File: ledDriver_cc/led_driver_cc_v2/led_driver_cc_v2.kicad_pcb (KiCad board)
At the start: 2 copper layers, 97 x 72 mm, 21 parts, among them J1 Conn_01x08_Pin, J3 Conn_01x02_Female, U1 TSR_1-2490, U2 WeMos_D1_mini

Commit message: add partslib
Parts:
- removed U7: ~, Package_SO:SOIC-8_3.9x4.9mm_P1.27mm
- added ESP32_S1: ~, custom_footprints:ESP32-S3-Zero, F.Cu at (101.4, 124.5)
- added H1: MountingHole, MountingHole:MountingHole_2.7mm_M2.5_DIN965_Pad_TopBottom, F.Cu at (92.9, 89.5)
- added H2: MountingHole, MountingHole:MountingHole_2.7mm_M2.5_DIN965_Pad_TopBottom, F.Cu at (175.9, 138.5)
- added H3: MountingHole, MountingHole:MountingHole_2.7mm_M2.5_DIN965_Pad_TopBottom, F.Cu at (175.9, 89.5)
- added H4: MountingHole, MountingHole:MountingHole_2.7mm_M2.5_DIN965_Pad_TopBottom, F.Cu at (92.9, 139.0)
- U2: value WeMos_D1_mini -> LM3404; footprint Module:WEMOS_D1_mini_light -> Package_SO:SOIC-8_3.9x4.9mm_P1.27mm
- moved C14 71.2 mm to (139.4, 134.9)
- moved R19 65.3 mm to (145.9, 123.0), turned to 180 degrees
- moved U2 59.6 mm to (146.2, 130.0), turned to 90 degrees
- moved C11 58.4 mm to (135.4, 134.5)
- moved C1 48.2 mm to (102.4, 109.5)
- moved R3 47.0 mm to (162.9, 127.5)
- moved C12 43.5 mm to (102.4, 111.1)
- moved C10 35.8 mm to (94.8, 109.4)
- moved C13 35.8 mm to (99.4, 109.5)
- moved D2 26.7 mm to (146.1, 137.5)
- moved L2 25.4 mm to (157.9, 135.5)
- moved C2 19.3 mm to (122.8, 94.5)
- moved C3 19.3 mm to (129.3, 109.7)
- moved C4 19.3 mm to (136.8, 94.5)
- moved C5 19.3 mm to (122.3, 110.5)
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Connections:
- C1 pad 1: Net-(U7-VCC) -> Net-(U2-VCC)
- C14 pad 1: Net-(U7-BOOT) -> Net-(U2-BOOT)
- C3 pad 1: VCC -> +5V
- C5 pad 1: VCC -> +5V
- R19 pad 1: Net-(U7-RON) -> Net-(U2-RON)
- U1 pad 3: VCC -> +5V
- U2 pad 1: unconnected-(U2-~{RST}-Pad1) -> Net-(D2-K)
- U2 pad 2: unconnected-(U2-A0-Pad2) -> Net-(U2-BOOT)
- U2 pad 3: unconnected-(U2-D0-Pad3) -> PWM3
- U2 pad 4: unconnected-(U2-SCK/D5-Pad4) -> GND
- U2 pad 6: unconnected-(U2-MOSI/D7-Pad6) -> Net-(U2-RON)
- U2 pad 7: unconnected-(U2-CS/D8-Pad7) -> Net-(U2-VCC)
- U2 pad 8: unconnected-(U2-3V3-Pad8) -> VCC
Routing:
- net Net-(D2-K): track 0.00 -> 16.0 mm
- net VCC: track 0.00 -> 4.75 mm
- net Net-(U2-RON): track 0.00 -> 4.53 mm
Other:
- board size 97 x 72 mm -> 89 x 55.5 mm

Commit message: more custom parts
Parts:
- F1: footprint Fuse:Fuseholder_Littelfuse_Nano2_154x -> custom_footprints:Fuse_Littelfuse-NANO2-451_453
- L2: footprint Inductor_SMD:L_10.4x10.4_H4.8 -> Inductor_SMD:L_TDK_SLF10145
- moved F1 0.80 mm to (108.4, 95.0)

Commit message: removed lib
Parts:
- C2: footprint Capacitor_THT:CP_Radial_D13.0mm_P5.00mm -> Capacitor_SMD:CP_Elec_10x10
- moved C4 4.98 mm to (141.8, 94.5)
- moved R3 4.83 mm to (158.1, 127.2)
- moved C2 4.43 mm to (123.3, 98.9)
- moved ESP32_S1 3.61 mm to (105.0, 124.9)
- moved J3 2.19 mm to (95.3, 101.8)

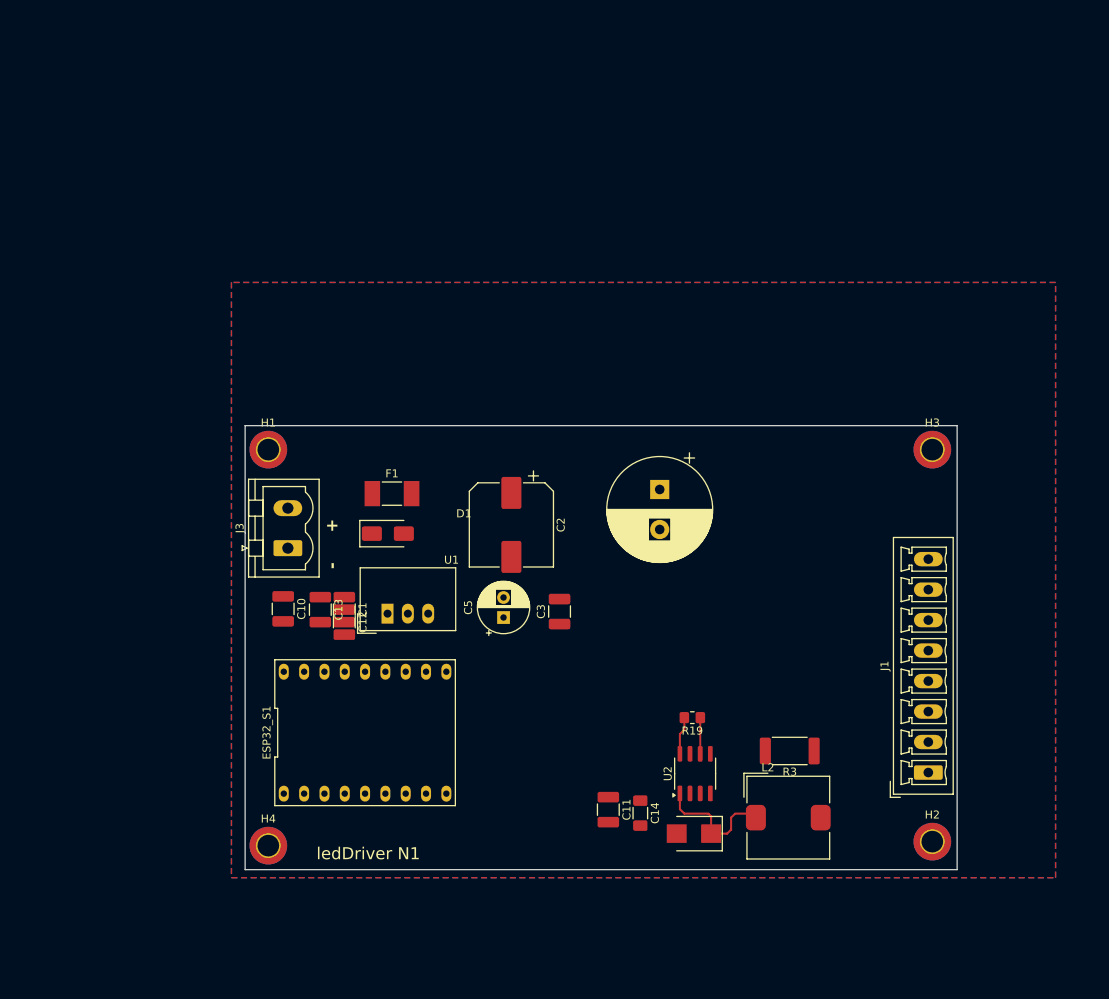
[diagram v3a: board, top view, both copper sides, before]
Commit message: add new channels to led driver
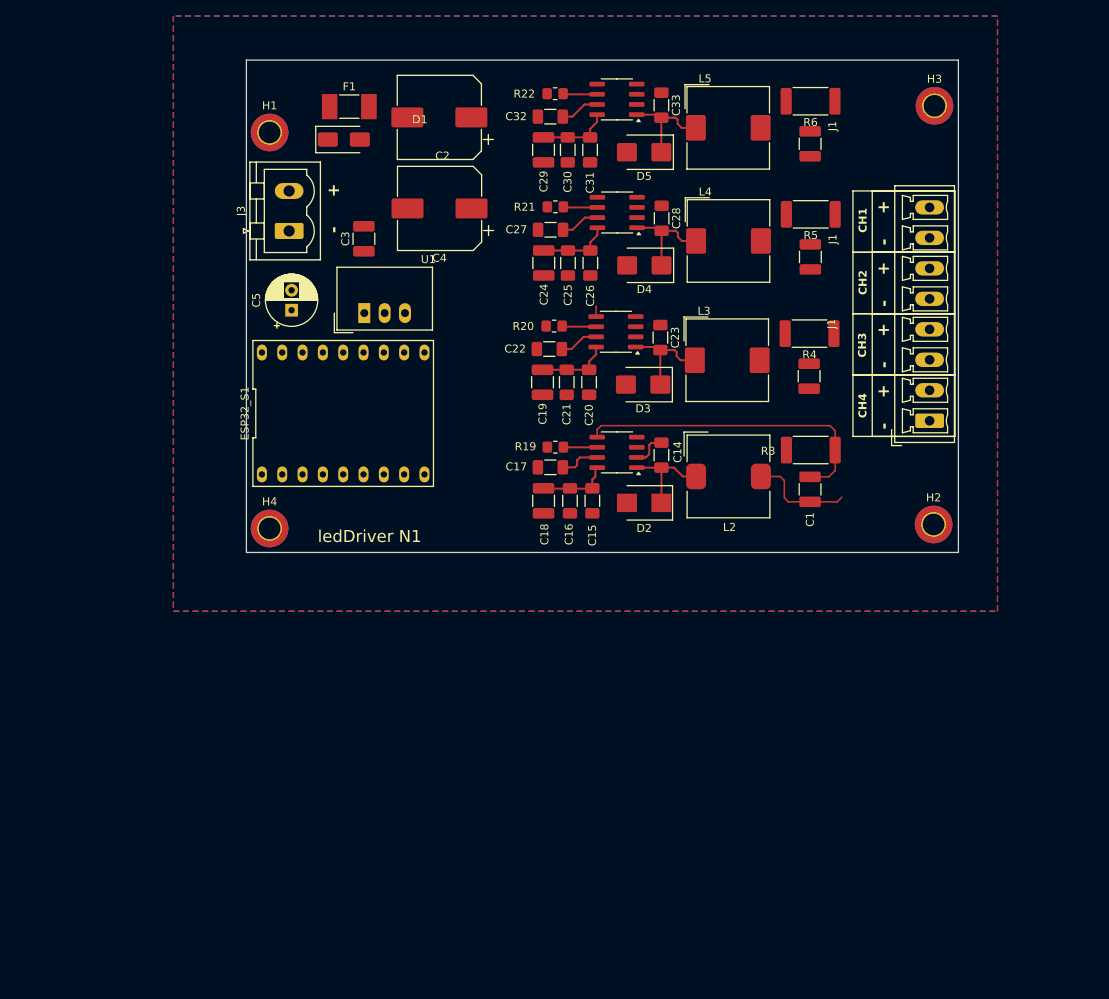
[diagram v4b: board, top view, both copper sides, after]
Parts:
- removed C10, C11, C12, C13: C, Capacitor_SMD:C_1210_3225Metric_Pad1.33x2.70mm_HandSolder
- added C15: 2,2UF, Capacitor_SMD:C_1206_3216Metric_Pad1.33x1.80mm_HandSolder, F.Cu at (133.4, 95.9)
- added C16: 100nF, Capacitor_SMD:C_1206_3216Metric_Pad1.33x1.80mm_HandSolder, F.Cu at (130.6, 95.9)
- added C17: 100nF, Capacitor_SMD:C_1206_3216Metric_Pad1.33x1.80mm_HandSolder, F.Cu at (128.2, 91.7)
- added C18: 10uF, Capacitor_SMD:C_1210_3225Metric_Pad1.33x2.70mm_HandSolder, F.Cu at (127.3, 95.9)
- added C19: 10uF, Capacitor_SMD:C_1210_3225Metric_Pad1.33x2.70mm_HandSolder, F.Cu at (127.2, 81.1)
- added C20: 2,2UF, Capacitor_SMD:C_1206_3216Metric_Pad1.33x1.80mm_HandSolder, F.Cu at (133.0, 81.1)
- added C21: 100nF, Capacitor_SMD:C_1206_3216Metric_Pad1.33x1.80mm_HandSolder, F.Cu at (130.2, 81.1)
- added C22: 100nF, Capacitor_SMD:C_1206_3216Metric_Pad1.33x1.80mm_HandSolder, F.Cu at (128.0, 76.9)
- added C23: 10nF, Capacitor_SMD:C_1206_3216Metric_Pad1.33x1.80mm_HandSolder, F.Cu at (141.9, 75.5)
- added C24: 10uF, Capacitor_SMD:C_1210_3225Metric_Pad1.33x2.70mm_HandSolder, F.Cu at (127.3, 66.2)
- added C25: 2,2UF, Capacitor_SMD:C_1206_3216Metric_Pad1.33x1.80mm_HandSolder, F.Cu at (130.4, 66.2)
- added C26: 100nF, Capacitor_SMD:C_1206_3216Metric_Pad1.33x1.80mm_HandSolder, F.Cu at (133.2, 66.2)
- added C27: 100nF, Capacitor_SMD:C_1206_3216Metric_Pad1.33x1.80mm_HandSolder, F.Cu at (128.2, 62.0)
- added C28: 10nF, Capacitor_SMD:C_1206_3216Metric_Pad1.33x1.80mm_HandSolder, F.Cu at (142.1, 60.6)
- added C29: 10uF, Capacitor_SMD:C_1210_3225Metric_Pad1.33x2.70mm_HandSolder, F.Cu at (127.3, 52.0)
- added C30: 2,2UF, Capacitor_SMD:C_1206_3216Metric_Pad1.33x1.80mm_HandSolder, F.Cu at (130.3, 52.0)
- added C31: 100nF, Capacitor_SMD:C_1206_3216Metric_Pad1.33x1.80mm_HandSolder, F.Cu at (133.1, 52.0)
- added C32: 100nF, Capacitor_SMD:C_1206_3216Metric_Pad1.33x1.80mm_HandSolder, F.Cu at (128.2, 47.9)
- added C33: 10nF, Capacitor_SMD:C_1206_3216Metric_Pad1.33x1.80mm_HandSolder, F.Cu at (142.0, 46.4)
- added C6: 470nF, Capacitor_SMD:C_1210_3225Metric_Pad1.33x2.70mm_HandSolder, F.Cu at (160.5, 80.3)
- added C7: 470nF, Capacitor_SMD:C_1210_3225Metric_Pad1.33x2.70mm_HandSolder, F.Cu at (160.7, 65.4)
- added C8: 470nF, Capacitor_SMD:C_1210_3225Metric_Pad1.33x2.70mm_HandSolder, F.Cu at (160.6, 51.3)
- added D3: D_Schottky, Diode_SMD:D_SMB, F.Cu at (139.7, 81.4)
- added D4: D_Schottky, Diode_SMD:D_SMB, F.Cu at (139.9, 66.5)
- added D5: D_Schottky, Diode_SMD:D_SMB, F.Cu at (139.9, 52.3)
- added L3: 47µH, Inductor_SMD:L_TDK_SLF10145, F.Cu at (150.3, 78.3)
- added L4: 47µH, Inductor_SMD:L_TDK_SLF10145, F.Cu at (150.4, 63.4)
- added L5: 47µH, Inductor_SMD:L_TDK_SLF10145, F.Cu at (150.4, 49.3)
- added R20: 536k, Resistor_SMD:R_0805_2012Metric_Pad1.20x1.40mm_HandSolder, F.Cu at (128.6, 74.1)
- added R21: 536k, Resistor_SMD:R_0805_2012Metric_Pad1.20x1.40mm_HandSolder, F.Cu at (128.8, 59.1)
- added R22: 536k, Resistor_SMD:R_0805_2012Metric_Pad1.20x1.40mm_HandSolder, F.Cu at (128.8, 45.0)
- added R4: 0.2R, Resistor_SMD:R_2512_6332Metric_Pad1.40x3.35mm_HandSolder, F.Cu at (160.6, 75.0)
- added R5: 0.2R, Resistor_SMD:R_2512_6332Metric_Pad1.40x3.35mm_HandSolder, F.Cu at (160.7, 60.1)
- added R6: 0.2R, Resistor_SMD:R_2512_6332Metric_Pad1.40x3.35mm_HandSolder, F.Cu at (160.7, 45.9)
- added U3: LM3404, Package_SO:SOIC-8_3.9x4.9mm_P1.27mm, F.Cu at (136.4, 74.8)
- added U4: LM3404, Package_SO:SOIC-8_3.9x4.9mm_P1.27mm, F.Cu at (136.5, 59.9)
- added U5: LM3404, Package_SO:SOIC-8_3.9x4.9mm_P1.27mm, F.Cu at (136.5, 45.7)
- C1: value C -> 470nF
- C14: value C -> 10nF
- C4: footprint Capacitor_THT:CP_Radial_D13.0mm_P5.00mm -> Capacitor_SMD:CP_Elec_10x10
- L2: value L -> 47µH
- R19: value R -> 536k
- R3: value R -> 0.2R
- moved C1 60.1 mm to (160.6, 94.5), turned to 90 degrees
- moved C3 52.6 mm to (104.8, 63.1)
- moved C2 51.7 mm to (114.3, 48.0), turned to 180 degrees
- moved D1 49.6 mm to (102.3, 50.7)
- moved F1 48.7 mm to (103.0, 46.6)
- moved C5 46.7 mm to (95.8, 72.1)
- moved C14 44.8 mm to (142.0, 90.2)
- moved C4 44.6 mm to (114.3, 59.3), turned to 180 degrees
- moved J1 44.0 mm to (175.6, 85.9)
- moved L2 43.3 mm to (150.4, 92.9)
- moved H3 43.0 mm to (176.2, 46.5)
- moved D2 41.8 mm to (139.9, 96.2)
- moved U2 41.3 mm to (136.5, 89.8), turned to 180 degrees
- moved ESP32_S1 40.0 mm to (102.3, 85.0)
- moved H1 39.6 mm to (93.1, 49.9)
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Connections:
- net Net-(D2-K) renamed /U2_SW
- net Net-(U2-BOOT) renamed /U2_BOOT
- net PWM4 renamed PWM_CH4
- C1 pad 1: Net-(U2-VCC) -> LED_CH1+
- C1 pad 2: GND -> LED_CH1-
- ESP32_S1 pad 14: PWM3 -> PWM_CH3
- ESP32_S1 pad 15: PWM2 -> PWM_CH2
- ESP32_S1 pad 16: PWM1 -> PWM_CH1
- L2 pad 2: LED3+ -> LED_CH1+
- R3 pad 1: LED3- -> LED_CH1-
- U2 pad 3: PWM3 -> PWM_CH1
- U2 pad 5: unconnected-(U2-CS-Pad5) -> LED_CH1-
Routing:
- net LED_CH1-: track 0.00 -> 39.6 mm
- net VCC: track 4.75 -> 36.1 mm
- net /U4_SW: track 0.00 -> 25.4 mm
- net LED_CH1+: track 0.00 -> 12.9 mm
- net /U3_SW: track 0.00 -> 12.7 mm
- net Net-(U2-VCC): track 0.00 -> 4.95 mm
- net /U2_BOOT: track 0.00 -> 4.74 mm
- net Net-(U3-VCC): track 0.00 -> 4.54 mm
- net Net-(U5-VCC): track 0.00 -> 4.54 mm
- net Net-(U4-VCC): track 0.00 -> 4.54 mm
- net Net-(U4-RON): track 0.00 -> 4.36 mm
- net Net-(U3-RON): track 0.00 -> 4.36 mm
- net Net-(U5-RON): track 0.00 -> 4.36 mm
- net /U2_SW: track 16.0 -> 12.4 mm
- net LED_CH2-: track 0.00 -> 1.28 mm
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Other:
- board size 89 x 55.5 mm -> 89 x 61.5 mm
- board text added: "CH1"
- board text added: "CH2"
- board text added: "CH3"
- board text added: "CH4"
- board text added: "J1"

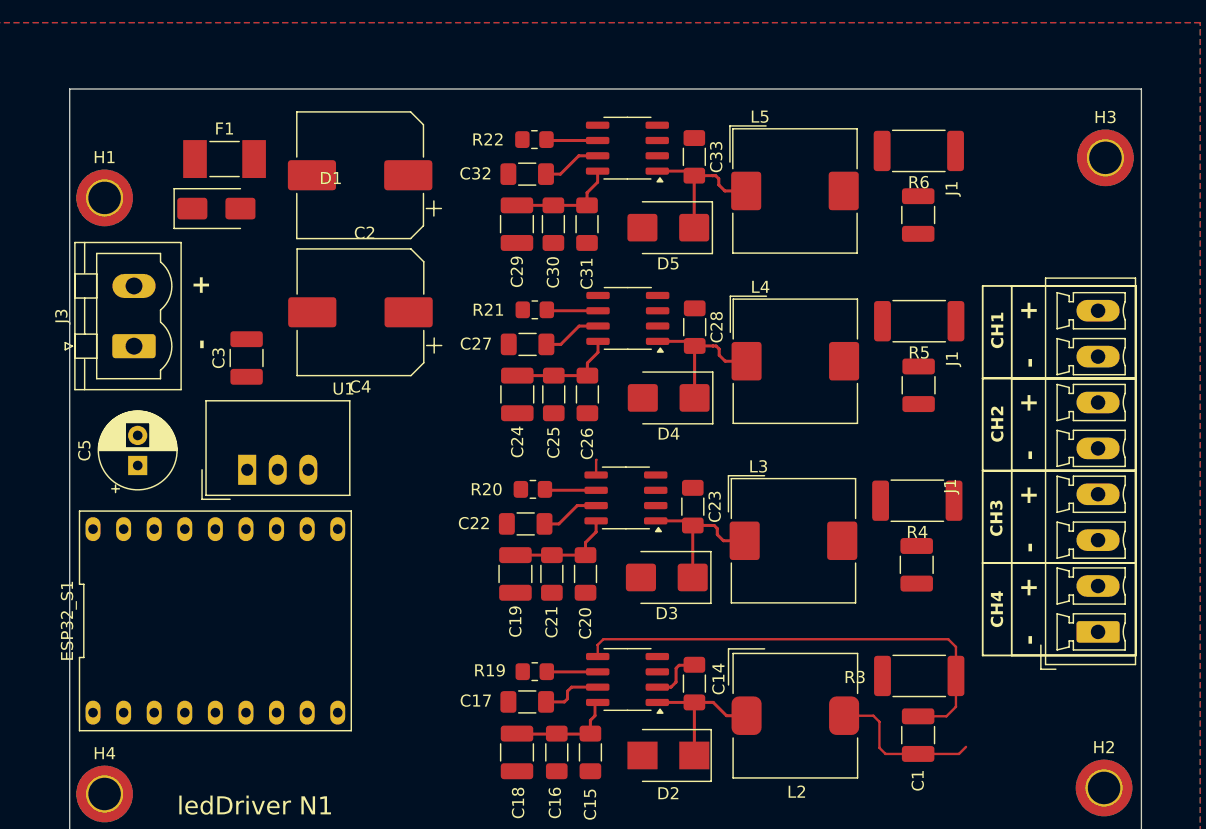
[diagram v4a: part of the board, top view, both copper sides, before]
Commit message: new channel arrangement
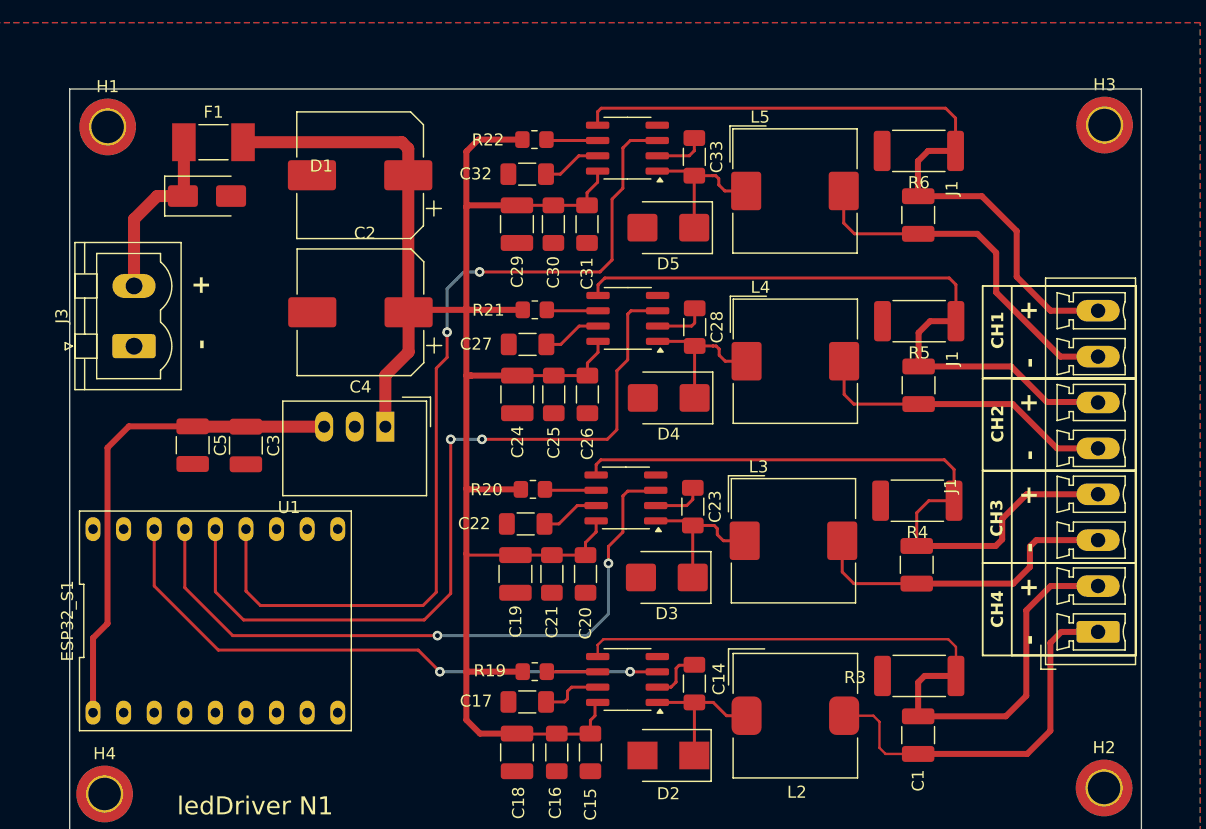
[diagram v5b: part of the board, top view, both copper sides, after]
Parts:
- C5: value C_Polarized -> C; footprint Capacitor_THT:CP_Radial_D6.3mm_P2.50mm -> Capacitor_SMD:C_1210_3225Metric_Pad1.33x2.70mm_HandSolder
- moved U1 12.0 mm to (116.4, 68.8), turned to 180 degrees
- moved C3 7.27 mm to (104.8, 70.4), turned to -90 degrees
- moved H1 5.90 mm to (93.3, 44.0)
- moved C5 4.87 mm to (100.4, 70.4), turned to -90 degrees
- moved H3 2.72 mm to (176.1, 43.8)
- moved F1 1.67 mm to (102.1, 45.2)
- moved D1 1.30 mm to (101.6, 49.7)
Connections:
- C1 pad 1: LED_CH1+ -> LED_CH4+
- C1 pad 2: LED_CH1- -> LED_CH4-
- C2 pad 1: Net-(U1-Vin) -> VCC
- C33 pad 1: /U4_BOOT -> /U5_BOOT
- C33 pad 2: /U4_SW -> /U5_SW
- C4 pad 1: Net-(U1-Vin) -> VCC
- C6 pad 1: LED_CH2+ -> LED_CH3+
- C6 pad 2: LED_CH2- -> LED_CH3-
- C7 pad 1: LED_CH3+ -> LED_CH2+
- C7 pad 2: LED_CH3- -> LED_CH2-
- C8 pad 1: LED_CH3+ -> LED_CH1+
- C8 pad 2: LED_CH3- -> LED_CH1-
- D5 pad 1: /U4_SW -> /U5_SW
- F1 pad 2: Net-(U1-Vin) -> VCC
- J1 pad 1: LED3- -> LED_CH4+
- J1 pad 2: LED3+ -> LED_CH4-
- J1 pad 3: LED4- -> LED_CH3+
- J1 pad 4: LED4+ -> LED_CH3-
- J1 pad 5: LED2+ -> LED_CH2+
- J1 pad 6: LED2- -> LED_CH2-
- J1 pad 7: LED1+ -> LED_CH1+
- J1 pad 8: LED1- -> LED_CH1-
- L2 pad 2: LED_CH1+ -> LED_CH4+
- L3 pad 2: LED_CH2+ -> LED_CH3+
- L4 pad 2: LED_CH3+ -> LED_CH2+
- L5 pad 1: /U4_SW -> /U5_SW
- L5 pad 2: LED_CH3+ -> LED_CH1+
- R3 pad 1: LED_CH1- -> LED_CH4-
- R4 pad 1: LED_CH2- -> LED_CH3-
- R5 pad 1: LED_CH3- -> LED_CH2-
- R6 pad 1: LED_CH3- -> LED_CH1-
- U1 pad 1: Net-(U1-Vin) -> VCC
- U2 pad 5: LED_CH1- -> LED_CH4-
- U3 pad 5: LED_CH2- -> LED_CH3-
- U4 pad 5: LED_CH3- -> LED_CH2-
- U5 pad 1: /U4_SW -> /U5_SW
- U5 pad 2: /U4_BOOT -> /U5_BOOT
- U5 pad 3: PWM_CH3 -> PWM_CH4
- U5 pad 5: LED_CH3- -> LED_CH1-
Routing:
- net VCC: track 36.1 -> 162.5 mm
- net PWM_CH4: track 0.00 -> 74.9 mm, vias 0 -> 2
- net PWM_CH3: track 0.00 -> 66.1 mm, vias 0 -> 2
- net LED_CH4-: track 0.00 -> 63.3 mm
- net LED_CH3-: track 0.00 -> 57.8 mm
- net PWM_CH2: track 0.00 -> 55.7 mm, vias 0 -> 2
- net LED_CH2-: track 1.28 -> 56.5 mm
- net PWM_CH1: track 0.00 -> 49.7 mm, vias 0 -> 2
- net +5V: track 0.00 -> 41.2 mm
- net LED_CH4+: track 0.00 -> 32.1 mm
- net LED_CH3+: track 0.00 -> 26.7 mm
- net LED_CH2+: track 0.00 -> 25.7 mm
- net LED_CH1-: track 39.6 -> 61.5 mm
- net LED_CH1+: track 12.9 -> 30.3 mm
- net Net-(D1-A1): track 0.00 -> 14.9 mm
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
